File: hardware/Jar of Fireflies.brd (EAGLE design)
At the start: 81.3 x 81.3 mm, 31 parts, among them IC1 ATTINY85, J1 PJ-006A, J3 SENSOR, J4 ICSP

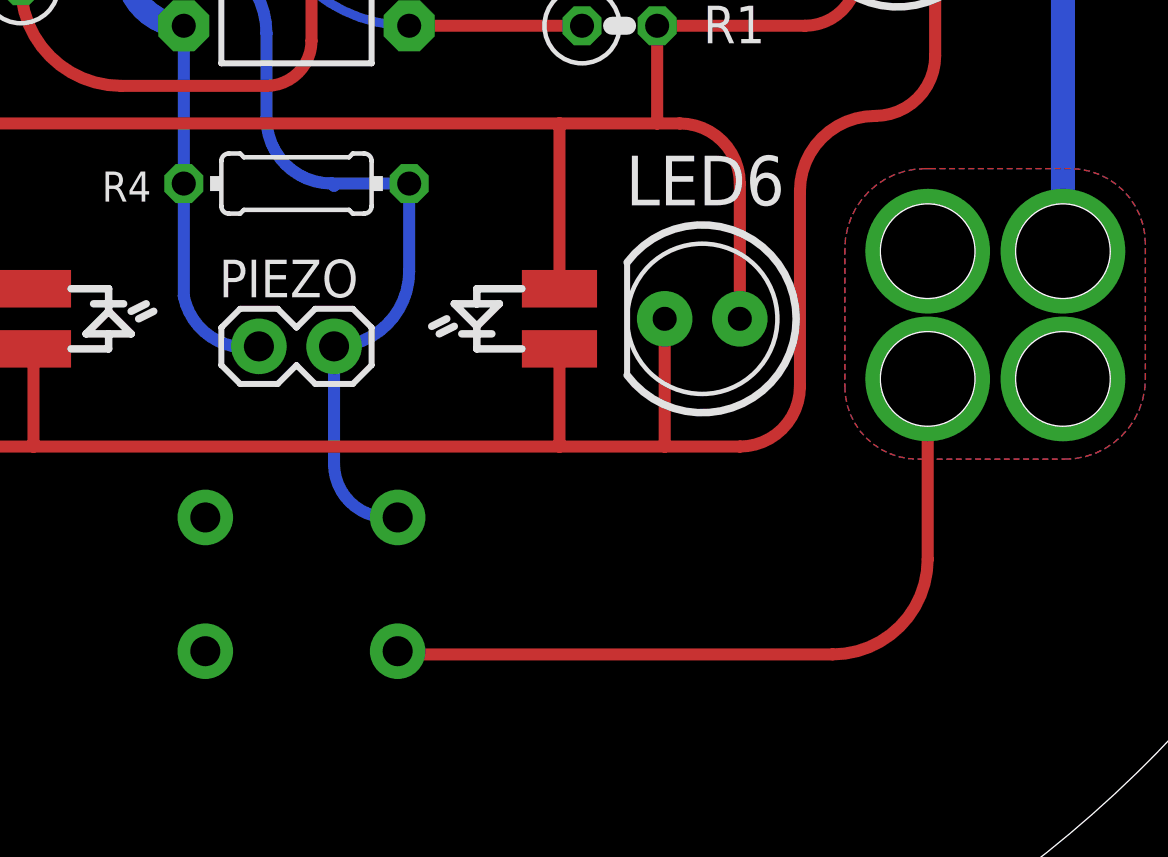
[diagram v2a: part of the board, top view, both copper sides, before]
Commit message: Replacing pushbutton with sourced one
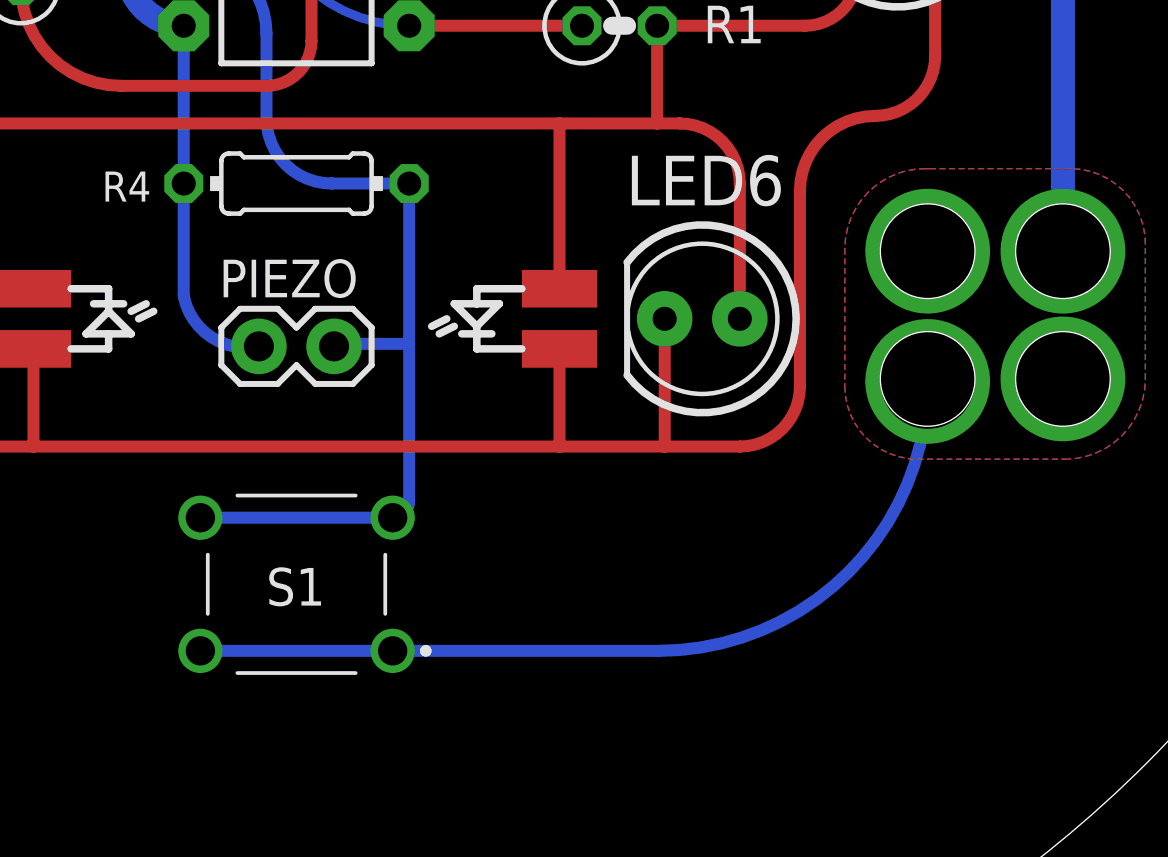
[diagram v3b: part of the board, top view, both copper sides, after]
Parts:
- S1: value (none) -> 1825910-7; device SparkFun-Electromechanical:TACTILE-PTH -> 1825910-7:SW_1825910-7
- moved S1 0.17 mm to (40.6, 18.0), flipped to the top, turned to 180 degrees
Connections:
- removed net N$2: PIEZO.2, R4.2, S1.1
- removed net PIEZO: IC1.3
- new net DANCE: IC1.3, PIEZO.2, R4.2, S1.3, S1.4
- net VCC: now also S1.1, S1.2; no longer S1.3
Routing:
- net DANCE: track 0.00 -> 33.2 mm
- net N$2: track 13.4 -> 0.00 mm
- net PIEZO: track 12.7 -> 0.00 mm
- net VCC: track 129.6 -> 132.5 mm
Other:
- board text removed: "Silkscreen artwork is on layer 200"
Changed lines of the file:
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@@
 <hole x="66.548" y="24.892" drill="3.2"/>
 <text x="44.788684375" y="55.11835625" size="1.27" layer="27" font="vector" ratio="12" rot="R90">10uF</text>
-<text x="91.186" y="42.418" size="1.778" layer="52">Silkscreen artwork is on layer 200</text>
 <wire x1="22.352" y1="54.864" x2="20.828" y2="54.864" width="0.254" layer="21"/>
 <wire x1="20.828" y1="54.864" x2="20.828" y2="54.356" width="0.254" layer="21"/>
@@
 <attribute name="NAME" x="37.592" y="56.515353125" size="1.27" layer="25" font="vector" ratio="12" rot="R90"/>
 </element>
-<element name="S1" library="SparkFun-Electromechanical" package="TACTILE-PTH" value="" x="40.809340625" y="17.94934375" smashed="yes" rot="MR0">
-<attribute name="PROD_ID" value=" SWCH-08441" x="40.809340625" y="17.94934375" size="1.778" layer="28" rot="MR0" display="off"/>
-</element>
 <element name="PAD1" library="wirepad" package="SMD1,27-2,54" value="" x="23.622" y="52.832" smashed="yes" rot="R270">
 <attribute name="VALUE" x="23.622" y="52.832" size="0.0254" layer="27" rot="R270"/>
@@
 </element>
 <element name="J2" library="SparkFun-Connectors" package="JST-2-PTH-VERT" value="" x="51.64924375" y="66.551328125" rot="MR270"/>
+<element name="S1" library="1825910-7" package="SW_1825910-7" value="1825910-7" x="40.64203125" y="17.950234375" smashed="yes" rot="R180">
+<attribute name="COMMENT" value="1825910-7" x="40.64203125" y="17.950234375" size="1.778" layer="27" rot="R180" display="off"/>
+<attribute name="CONFIGURATION_POLE-THROW" value="Single Pole - Single Throw" x="40.64203125" y="17.950234375" size="1.778" layer="27" rot="R180" display="off"/>
+<attribute name="CONTACT_CURRENT_RATING" value="50 mA" x="40.64203125" y="17.950234375" size="1.778" layer="27" rot="R180" display="off"/>
+<attribute name="DESCRIPTION" value=" FSM4JAH=6MM TACT SWITCH, HIGH TEMP " x="40.64203125" y="17.950234375" size="1.778" layer="27" rot="R180" display="off"/>
+<attribute name="DIGI-KEY_PART_NUMBER" value="450-1804-ND" x="40.64203125" y="17.950234375" size="1.778" layer="27" rot="R180" display="off"/>
+<attribute name="DIGI-KEY_PURCHASE_URL" value="https://www.digikey.com/product-detail/en/te-connectivity-alcoswitch-switches/1825910-7/450-1804-ND/1731414?utm_source=snapeda&amp;utm_medium=aggregator&amp;utm_campaign=symbol" x="40.64203125" y="17.950234375" size="1.778" layer="27" rot="R180" display="off"/>
+<attribute name="EU_ROHS_COMPLIANCE" value="Compliant" x="40.64203125" y="17.950234375" size="1.778" layer="27" rot="R180" display="off"/>
+<attribute name="LINK" value="http://www.te.com/usa-en/product-1825910-7.html" x="40.64203125" y="17.950234375" size="1.778" layer="27" rot="R180" display="off"/>
+<attribute name="MF" value="TE Connectivity" x="40.64203125" y="17.950234375" size="1.778" layer="27" rot="R180" display="off"/>
+<attribute name="MP" value="1825910-7" x="40.64203125" y="17.950234375" size="1.778" layer="27" rot="R180" display="off"/>
+<attribute name="NAME" x="41.612996875" y="18.503346875" size="1.27403125" layer="25" rot="R180"/>
+<attribute name="PACKAGE" value="None" x="40.64203125" y="17.950234375" size="1.778" layer="27" rot="R180" display="off"/>
+</element>
 </elements>
 <signals>
@@
 <via x="61.976" y="29.21" extent="1-16" drill="3.2"/>
 <via x="66.548" y="24.892" extent="1-16" drill="3.2"/>
-<via x="61.976" y="24.892" extent="1-16" drill="3.2"/>
 <polygon width="0.254" layer="1">
 <vertex x="66.626003125" y="22.180446875" curve="90"/>
@@
 <vertex x="61.631171875" y="22.180446875"/>
 </polygon>
-<contactref element="S1" pad="3"/>
-<wire x1="61.976" y1="24.892" x2="61.976" y2="18.79384375" width="0.4064" layer="1"/>
-<wire x1="61.976" y1="18.79384375" x2="58.761603125" y2="15.579446875" width="0.4064" layer="1" curve="-90"/>
-<wire x1="58.761603125" y1="15.579446875" x2="44.1698375" y2="15.579446875" width="0.4064" layer="1"/>
-<wire x1="44.1698375" y1="15.579446875" x2="44.060540625" y2="15.68874375" width="0.4064" layer="1" curve="-90"/>
 <contactref element="J4" pad="2"/>
 <wire x1="43.182290625" y1="51.9878" x2="43.182421875" y2="51.98793125" width="0.8128" layer="16" curve="-90"/>
@@
 <wire x1="66.548228125" y1="48.916953125" x2="66.548228125" y2="51.20234375" width="0.8128" layer="16"/>
 <wire x1="66.548228125" y1="51.20234375" x2="52.19924375" y2="65.551328125" width="0.8128" layer="16" curve="90"/>
+<contactref element="S1" pad="1"/>
+<contactref element="S1" pad="2"/>
+<via x="61.976" y="24.807115625" extent="1-16" drill="3.2"/>
+<wire x1="37.39203125" y1="15.700234375" x2="43.89203125" y2="15.700234375" width="0.4064" layer="16"/>
+<wire x1="43.89203125" y1="15.700234375" x2="52.86911875" y2="15.700234375" width="0.4064" layer="16"/>
+<wire x1="52.86911875" y1="15.700234375" x2="61.976" y2="24.807115625" width="0.4064" layer="16" curve="90"/>
 <wire x1="43.182159375" y1="51.987803125" x2="43.182290625" y2="51.9878" width="0" layer="19" extent="16-16"/>
 </signal>
@@
 <wire x1="40.642159375" y1="45.717840625" x2="44.45" y2="41.91" width="0.4064" layer="16" curve="90"/>
 </signal>
-<signal name="PIEZO">
+<signal name="DANCE">
 <contactref element="IC1" pad="3"/>
 <wire x1="36.83" y1="39.37" x2="39.62598125" y2="36.57401875" width="0.4064" layer="16" curve="-90"/>
 <wire x1="39.62598125" y1="36.57401875" x2="39.62598125" y2="33.69901875" width="0.4064" layer="16"/>
 <wire x1="39.62598125" y1="33.69901875" x2="41.827425" y2="31.497575" width="0.4064" layer="16" curve="90"/>
-<wire x1="41.827425" y1="31.497575" x2="44.448425" y2="31.497575" width="0.4064" layer="16"/>
-<wire x1="41.91" y1="31.415" x2="41.827425" y2="31.497575" width="0.4064" layer="16" curve="90"/>
+<wire x1="44.448425" y1="31.497575" x2="41.827425" y2="31.497575" width="0.4064" layer="16"/>
+<contactref element="S1" pad="4"/>
+<contactref element="S1" pad="3"/>
+<wire x1="37.39203125" y1="20.200234375" x2="43.89203125" y2="20.200234375" width="0.4064" layer="16"/>
+<wire x1="43.89203125" y1="20.200234375" x2="44.448425" y2="20.756628125" width="0.4064" layer="16" curve="90"/>
+<wire x1="44.448425" y1="20.756628125" x2="44.448425" y2="26.0786375" width="0.4064" layer="16"/>
+<contactref element="PIEZO" pad="2"/>
+<contactref element="R4" pad="2"/>
+<wire x1="44.448425" y1="26.0786375" x2="44.448425" y2="31.497575" width="0.4064" layer="16"/>
+<wire x1="41.91" y1="25.992709375" x2="41.995928125" y2="26.0786375" width="0.4064" layer="16" curve="-90"/>
+<wire x1="41.995928125" y1="26.0786375" x2="44.448425" y2="26.0786375" width="0.4064" layer="16"/>
+<wire x1="44.448425" y1="31.497575" x2="44.45" y2="31.496" width="0" layer="19" extent="16-16"/>
 </signal>
 <signal name="B">
@@
 <wire x1="33.19099375" y1="42.504790625" x2="33.19099375" y2="55.036084375" width="0.4064" layer="16"/>
 </signal>
-<signal name="N$2">
-<contactref element="PIEZO" pad="2"/>
-<contactref element="R4" pad="2"/>
-<contactref element="S1" pad="1"/>
-<wire x1="41.91" y1="22.0218" x2="41.91" y2="25.992709375" width="0.4064" layer="16"/>
-<wire x1="44.060540625" y1="20.20994375" x2="43.72185625" y2="20.20994375" width="0.4064" layer="16"/>
-<wire x1="43.72185625" y1="20.20994375" x2="41.91" y2="22.0218" width="0.4064" layer="16" curve="-90"/>
-<wire x1="41.91" y1="25.992709375" x2="44.45" y2="28.532709375" width="0.4064" layer="16" curve="90"/>
-<wire x1="44.45" y1="28.532709375" x2="44.45" y2="31.496" width="0.4064" layer="16"/>
-</signal>
 </signals>

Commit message: Flipping bitmap silkscreen
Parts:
- flipped R5 to the top
- flipped S1 to the bottom
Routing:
- net RESET: track 15.2 -> 11.5 mm
- net VCC: track 132.5 -> 132.3 mm, vias 5 -> 4

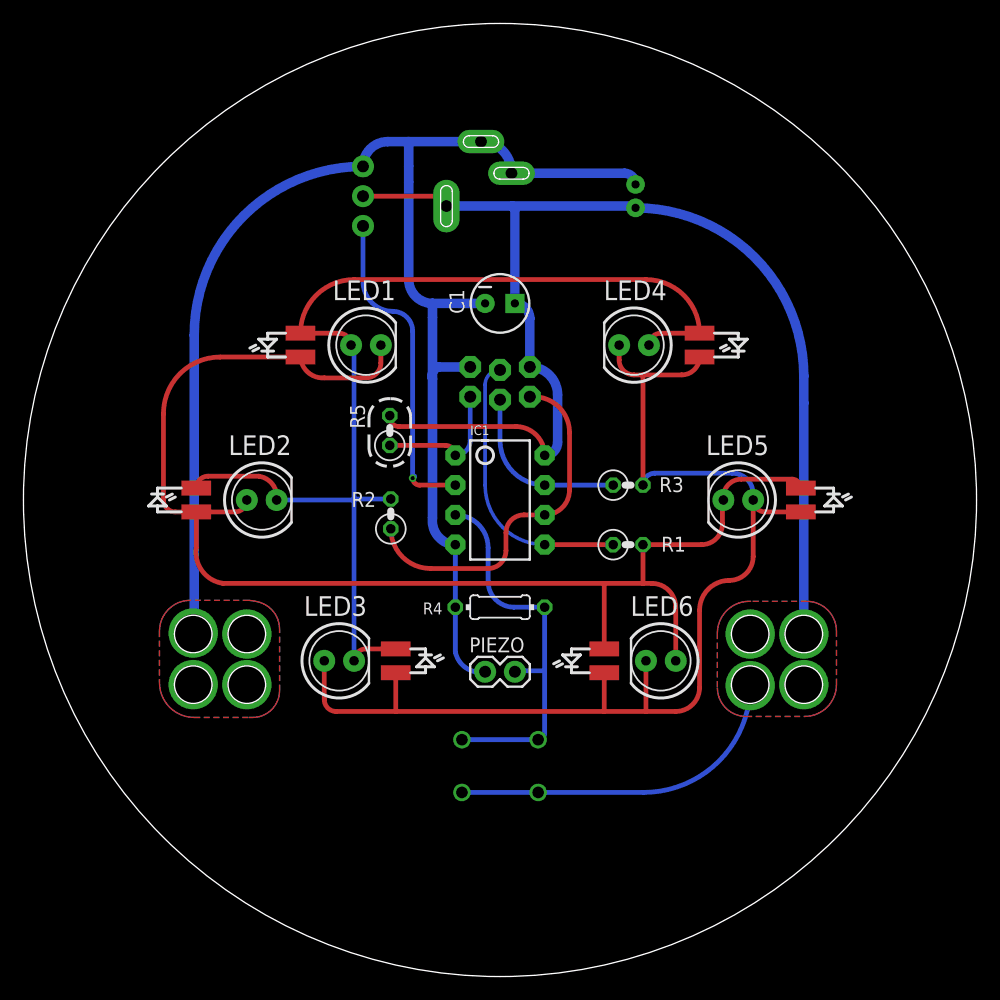
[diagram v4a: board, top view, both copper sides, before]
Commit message: Removing piezo from PCB, making button switch to GND, adding solder pads to sensor interface
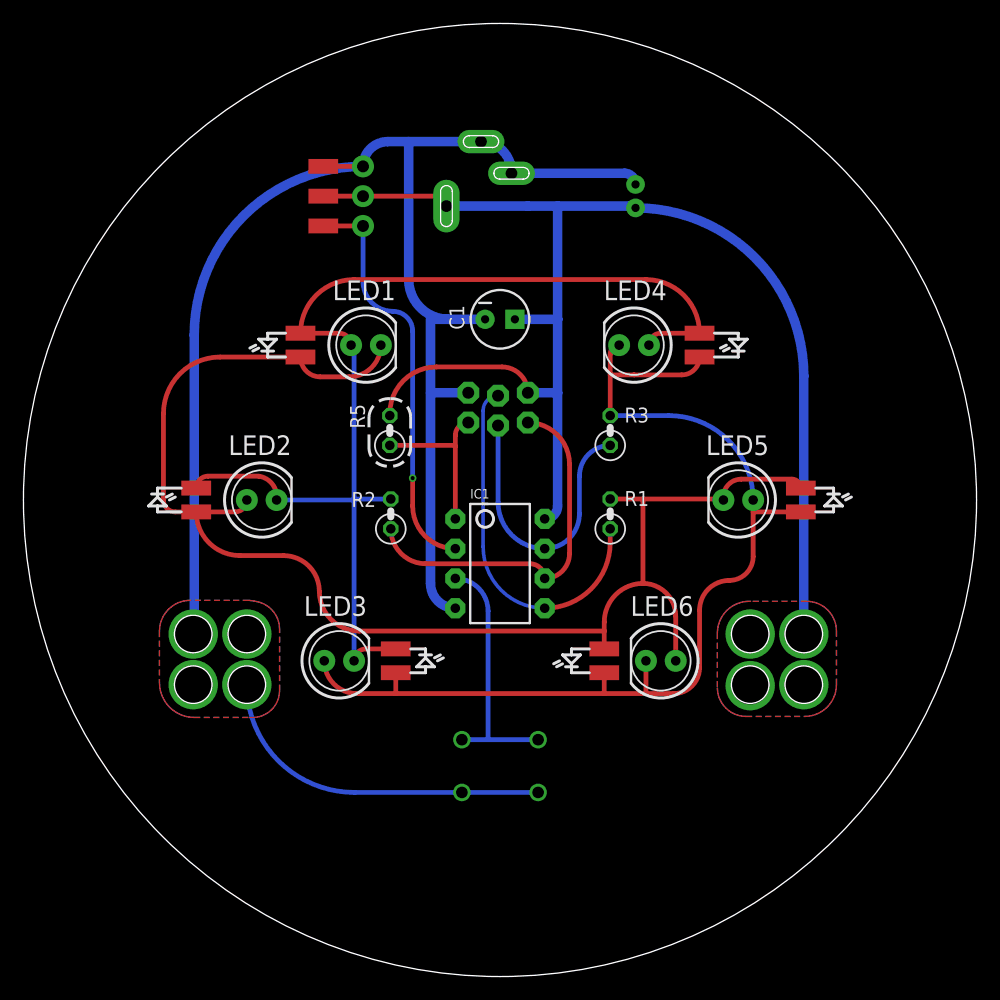
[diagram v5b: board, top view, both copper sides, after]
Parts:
- removed PIEZO: (no value), SparkFun:1X02
- removed R4: 1M, resistor:0204/7
- added PAD13, PAD14, PAD15: WIREPADSMD1,27-254, wirepad:SMD1,27-2,54
- J2: value (none) -> JST PH vertical
- LED1, LED2, LED3, LED4, LED5, LED6: value (none) -> Amber
- R1, R2, R3: value (none) -> 150
- moved IC1 5.42 mm to (40.6, 35.2)
- moved R3 4.90 mm to (50.0, 46.6), turned to 90 degrees
- moved R1 3.03 mm to (50.0, 39.5), turned to 90 degrees
- moved J4 2.21 mm to (43.0, 47.2)
- moved C1 1.35 mm to (40.6, 56.0)
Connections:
- net DANCE: no longer PIEZO.2, R4.2
- net GND: now also PAD13.1, S1.1, S1.2; no longer PIEZO.1, R4.1
- net SENSOR: now also PAD15.1
- net VCC: now also PAD14.1; no longer S1.1, S1.2
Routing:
- net GND: track 128.1 -> 153.5 mm
- net VCC: track 132.3 -> 117.1 mm
- net DANCE: track 33.2 -> 21.4 mm
- net C: track 99.6 -> 90.4 mm
- net SCK: track 14.7 -> 23.3 mm
- net SENSOR: track 27.4 -> 34.2 mm
- net MOSI: track 23.4 -> 29.9 mm
- net RESET: track 11.5 -> 14.3 mm
- net MISO: track 29.9 -> 30.5 mm
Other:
- board text added: "LED1"
- board text added: "LED2"
- board text added: "LED3"
- board text added: "LED4"
- board text added: "LED5"
- board text added: "LED6"
- board text added: "SIGNAL"
